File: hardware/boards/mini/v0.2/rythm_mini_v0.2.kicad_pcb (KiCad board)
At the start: 8 copper layers, 20 x 50 mm, 88 parts, among them IC1 NAU88C22YG, IC3 IS42S16160J-6BLI, J2 Bottom, J3 Top, Q1 PMV37EN22, U1 W25Q128JVP, U2 LTV-217-G, U4 STM32H750XBHx, Y1 Crystal_GND24

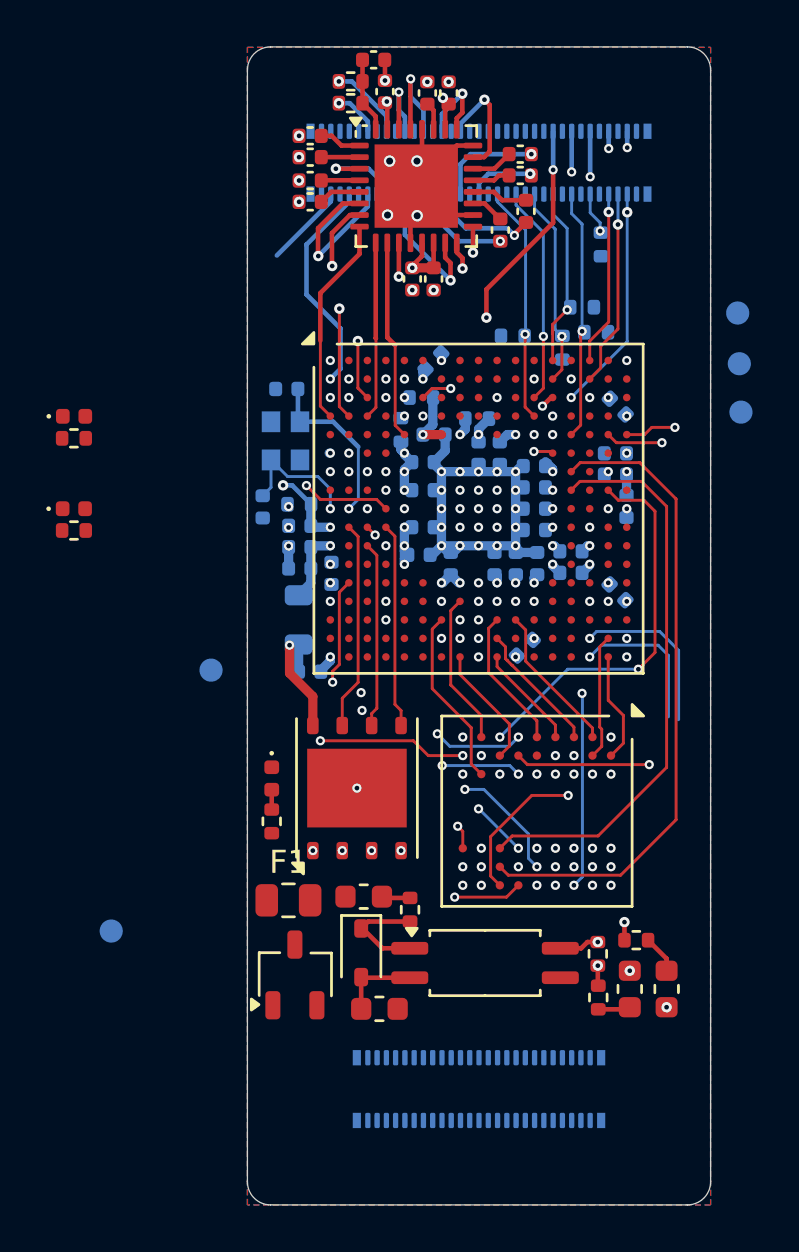
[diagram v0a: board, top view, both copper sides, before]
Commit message: mini: route more GPIO
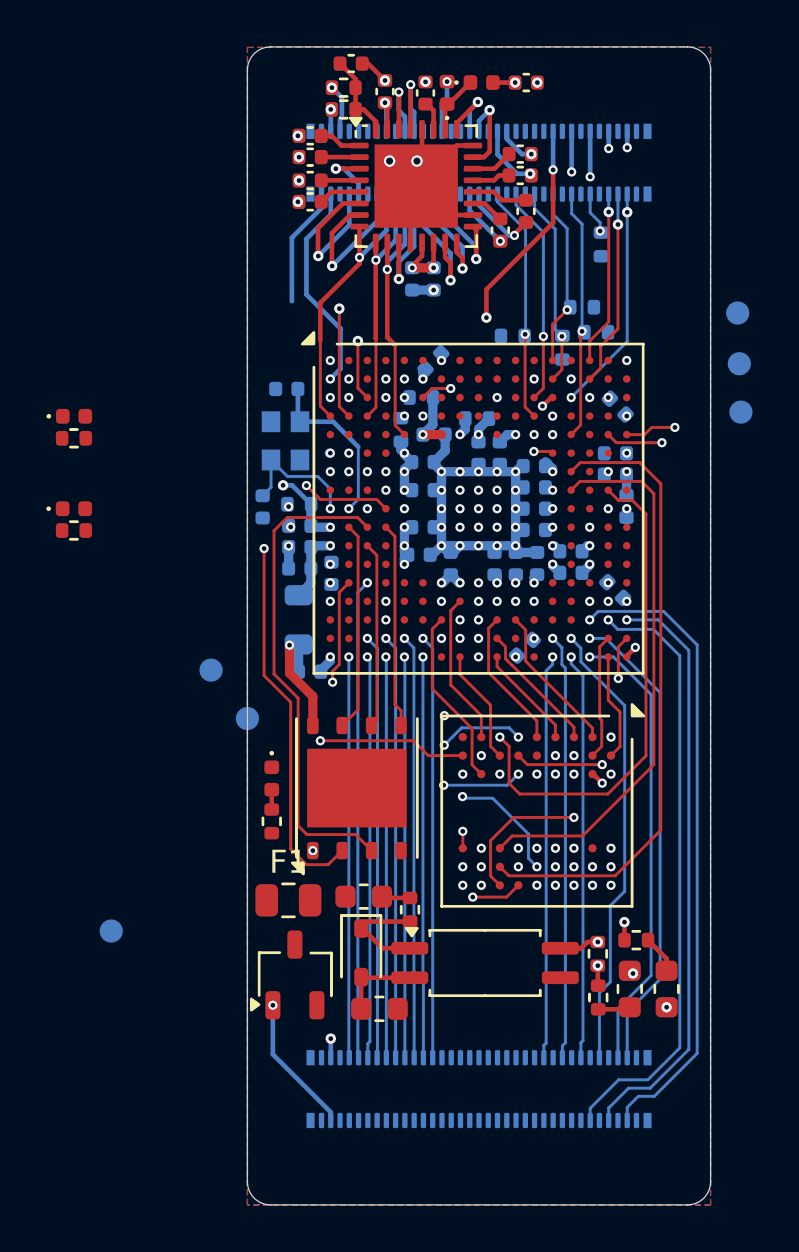
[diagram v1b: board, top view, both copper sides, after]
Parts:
- removed J2: Bottom, Connector_Hirose_DF40:Hirose_DF40C-50DP-0.4V_2x25-1MP_P0.4mm
- added D5: D, Diode_SMD:D_0402_1005Metric, F.Cu at (80.1, 56.5)
- added D6: D, Diode_SMD:D_0402_1005Metric, F.Cu at (78.6, 57.0)
- added J1: Bottom, Connector_Hirose_DF40:Hirose_DF40C-70DP-0.4V_2x35-1MP_P0.4mm, B.Cu at (80.0, 100.0)
- C16, C17: moved to B.Cu
- moved TP1 5.59 mm to (70.0, 84.0)
- moved C18 3.38 mm to (82.0, 56.5), turned to 0 degrees
- moved C28 0.98 mm to (74.5, 55.7)
- moved C16 0.92 mm to (78.0, 65.0)
- moved C17 0.92 mm to (77.1, 65.0)
- moved R3 0.40 mm to (74.2, 57.7)
- moved R4 0.40 mm to (74.2, 56.8)
- moved C60 0.14 mm to (85.9, 78.5)
- moved C29 0.08 mm to (77.7, 57.0)
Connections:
- IC1 pad 26: +3.3V -> Net-(D5-K)
- J3 pad 29: unconnected-(J3-Pad29) -> /AUX_OUT_L
- J3 pad 31: unconnected-(J3-Pad31) -> /AUX_OUT_R
- J3 pad 35: unconnected-(J3-Pad35) -> /SPKR
- J3 pad 36: /AUX_OUT_R -> /AUX_IN_R
- J3 pad 37: unconnected-(J3-Pad37) -> /SPKL
- J3 pad 38: unconnected-(J3-Pad38) -> /AUX_IN_L
- J3 pad 39: /SPKR -> unconnected-(J3-Pad39)
- J3 pad 40: /AUX_OUT_L -> unconnected-(J3-Pad40)
- J3 pad 42: unconnected-(J3-Pad42) -> /I2C_SDA
- J3 pad 43: /SPKL -> /VDDSPK
- J3 pad 44: /AUX_IN_R -> /I2C_SCL
- J3 pad 47: /HPR -> unconnected-(J3-Pad47)
- J3 pad 48: /AUX_IN_L -> /CODEC_GPIO
- J3 pad 49: unconnected-(J3-Pad49) -> /HPR
- J3 pad 50: unconnected-(J3-Pad50) -> /SAI1_MCLK
- J3 pad 52: /CODEC_GPIO -> /SAI1_SD_A
- J3 pad 54: unconnected-(J3-Pad54) -> /SAI1_SD_B
- J3 pad 55: /MICL -> +3.3V
- J3 pad 56: /LIN -> /SAI1_SCK
- J3 pad 58: unconnected-(J3-Pad58) -> /SAI1_FS
- J3 pad 59: /MICR -> unconnected-(J3-Pad59)
- J3 pad 60: /RIN -> unconnected-(J3-Pad60)
- J3 pad 62: unconnected-(J3-Pad62) -> /LIN
- J3 pad 64: /VBAT -> /RIN
- J3 pad 65: unconnected-(J3-Pad65) -> /MICL
- J3 pad 67: unconnected-(J3-Pad67) -> /MICR
- J3 pad 68: /RST -> /VBAT
- J3 pad 70: unconnected-(J3-Pad70) -> /RST
- U4 pad N3: unconnected-(U4A-PA2-PadN3) -> /PA2
- U4 pad R15: unconnected-(U4D-PD11-PadR15) -> /PD11
- U4 pad R16: unconnected-(U4D-PD12-PadR16) -> /PD12
- U4 pad R17: unconnected-(U4D-PD13-PadR17) -> /PD13
- U4 pad T13: unconnected-(U4H-PH8-PadT13) -> /PH8
- U4 pad T14: unconnected-(U4B-PB12-PadT14) -> /PB12
- U4 pad T3: unconnected-(U4A-PA5-PadT3) -> /PA5
- U4 pad T4: unconnected-(U4C-PC4-PadT4) -> /PC4
- U4 pad T5: unconnected-(U4B-PB1-PadT5) -> /PB1
- U4 pad T6: unconnected-(U4J-PJ2-PadT6) -> /PJ2
- U4 pad U13: unconnected-(U4H-PH7-PadU13) -> /PH7
- U4 pad U14: unconnected-(U4B-PB13-PadU14) -> /PB13
- U4 pad U2: unconnected-(U4A-PA3-PadU2) -> /PA3
- U4 pad U3: unconnected-(U4A-PA4-PadU3) -> /PA4
- U4 pad U4: unconnected-(U4C-PC5-PadU4) -> /PC5
- U4 pad U5: unconnected-(U4B-PB0-PadU5) -> /PB0
- U4 pad U6: unconnected-(U4J-PJ3-PadU6) -> /PJ3
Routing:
- net /PD11: track 0.00 -> 27.6 mm, vias 0 -> 1
- net /PD12: track 0.00 -> 26.1 mm, vias 0 -> 1
- net /PD13: track 0.00 -> 25.5 mm, vias 0 -> 1
- net /PA2: track 0.00 -> 20.7 mm, vias 0 -> 1
- net /PB12: track 0.00 -> 19.5 mm, vias 0 -> 1
- net /PH8: track 0.00 -> 18.4 mm, vias 0 -> 1
- net /PA5: track 0.00 -> 18.3 mm, vias 0 -> 1
- net /PJ2: track 0.00 -> 18.3 mm, vias 0 -> 1
- net /PC4: track 0.00 -> 18.3 mm, vias 0 -> 1
- net /PB1: track 0.00 -> 18.3 mm, vias 0 -> 1
- net /PB13: track 0.00 -> 17.6 mm, vias 0 -> 1
- net /PH7: track 0.00 -> 17.5 mm, vias 0 -> 1
- net /PA4: track 0.00 -> 17.4 mm, vias 0 -> 1
- net /PA3: track 0.00 -> 17.3 mm, vias 0 -> 1
- net /PC5: track 0.00 -> 17.3 mm, vias 0 -> 1
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
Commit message: mini: shorten bottom of board
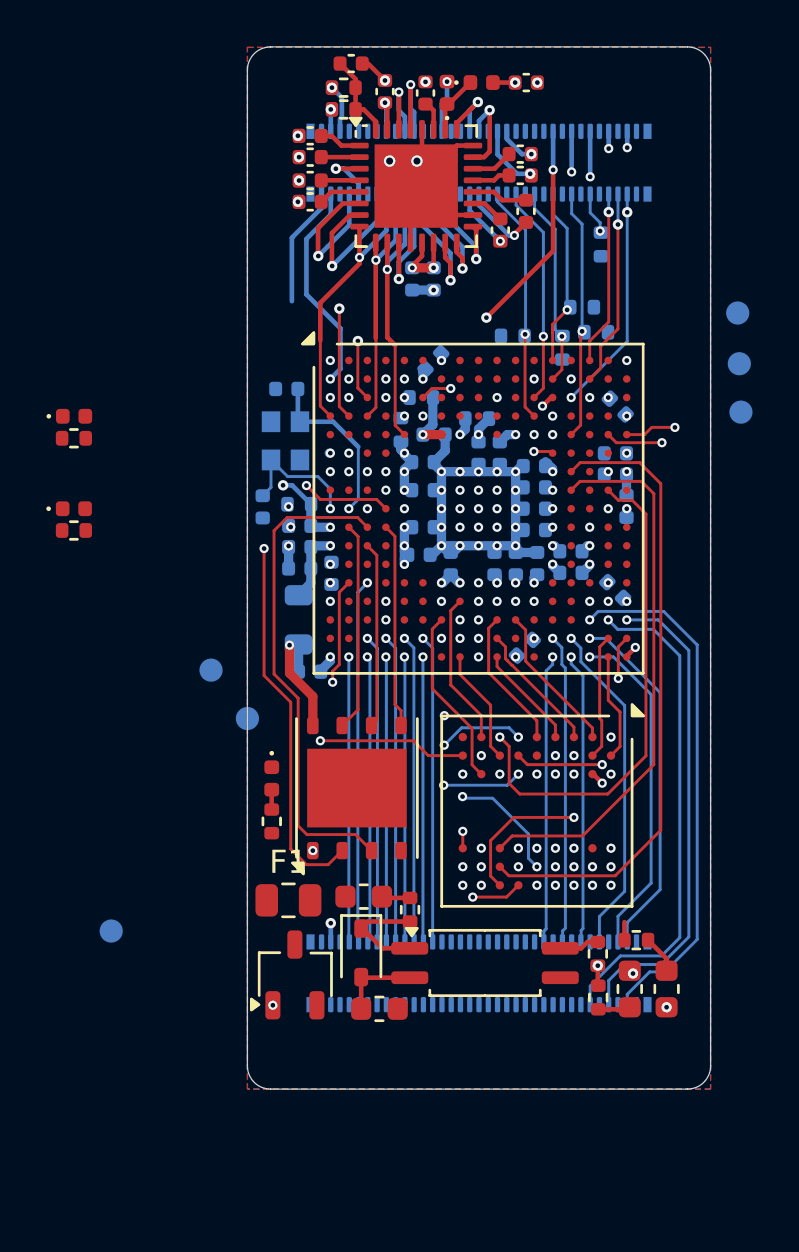
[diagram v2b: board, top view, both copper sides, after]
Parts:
- moved J1 5.00 mm to (80.0, 95.0)
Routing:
- net /3v3+: track 6.01 -> 0.00 mm
- net /PD11: track 27.6 -> 22.6 mm
- net /PH7: track 17.5 -> 12.5 mm
- net /PH8: track 18.4 -> 13.4 mm
- net /PC5: track 17.3 -> 12.3 mm
- net /PB0: track 17.3 -> 12.3 mm
- net /PA5: track 18.3 -> 13.3 mm
- net /USB_D-: track 19.6 -> 14.6 mm
- net /USB_D+: track 20.4 -> 15.4 mm
- net /PB13: track 17.6 -> 12.6 mm
- net /PB12: track 19.5 -> 14.5 mm
- net /PJ2: track 18.3 -> 13.3 mm
- net /PC4: track 18.3 -> 13.3 mm
- net /PB1: track 18.3 -> 13.3 mm
- net /PA3: track 17.3 -> 12.3 mm
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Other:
- board size 20 x 50 mm -> 20 x 45 mm
